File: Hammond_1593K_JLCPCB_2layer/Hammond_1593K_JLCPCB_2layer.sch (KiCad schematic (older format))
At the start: 2 parts

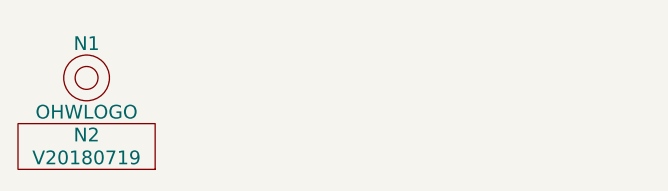
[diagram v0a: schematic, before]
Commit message: added Hammond 1593 PCB outline to template
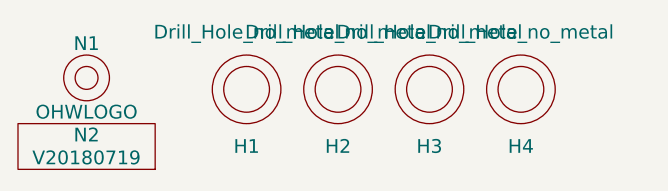
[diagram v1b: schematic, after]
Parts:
- added H1, H2, H3, H4: Drill_Hole_no_metal, SquantorPcbOutline:MountingHole_3.2mm_no_metal, symbol Drill_Hole_no_metal
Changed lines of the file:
@@
 LIBS:SquantorPCBOutline
 LIBS:SquantorProto
-LIBS:jlcpcb_2_layer-cache
+LIBS:Hammond_1593K_JLCPCB_2layer-cache
 EELAYER 25 0
 EELAYER END
@@
 	1    0    0    -1
 $EndComp
+$Comp
+L Drill_Hole_no_metal H1
+U 1 1 5B50D036
+P 1550 7400
+F 0 "H1" H 1550 7150 60  0000 C CNN
+F 1 "Drill_Hole_no_metal" H 1550 7650 60  0000 C CNN
+F 2 "SquantorPcbOutline:MountingHole_3.2mm_no_metal" H 1550 7400 60  0001 C CNN
+F 3 "" H 1550 7400 60  0001 C CNN
+	1    1550 7400
+	1    0    0    -1
+$EndComp
+$Comp
+L Drill_Hole_no_metal H2
+U 1 1 5B50D091
+P 1950 7400
+F 0 "H2" H 1950 7150 60  0000 C CNN
+F 1 "Drill_Hole_no_metal" H 1950 7650 60  0000 C CNN
+F 2 "SquantorPcbOutline:MountingHole_3.2mm_no_metal" H 1950 7400 60  0001 C CNN
+F 3 "" H 1950 7400 60  0001 C CNN
+	1    1950 7400
+	1    0    0    -1
+$EndComp
+$Comp
+L Drill_Hole_no_metal H3
+U 1 1 5B50D0D9
+P 2350 7400
+F 0 "H3" H 2350 7150 60  0000 C CNN
+F 1 "Drill_Hole_no_metal" H 2350 7650 60  0000 C CNN
+F 2 "SquantorPcbOutline:MountingHole_3.2mm_no_metal" H 2350 7400 60  0001 C CNN
+F 3 "" H 2350 7400 60  0001 C CNN
+	1    2350 7400
+	1    0    0    -1
+$EndComp
+$Comp
+L Drill_Hole_no_metal H4
+U 1 1 5B50D104
+P 2750 7400
+F 0 "H4" H 2750 7150 60  0000 C CNN
+F 1 "Drill_Hole_no_metal" H 2750 7650 60  0000 C CNN
+F 2 "SquantorPcbOutline:MountingHole_3.2mm_no_metal" H 2750 7400 60  0001 C CNN
+F 3 "" H 2750 7400 60  0001 C CNN
+	1    2750 7400
+	1    0    0    -1
+$EndComp

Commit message: updated Hammond 1593K JLCPCB 2 layer template
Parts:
- H1, H2, H3, H4: symbol Drill_Hole_no_metal -> SquantorPCBOutline:Drill_Hole_no_metal
- N1: symbol OHWLOGO -> SquantorLabels:OHWLOGO
- N2: value V20180719 -> 20180726; symbol VYYYYMMDD -> SquantorLabels:VYYYYMMDD
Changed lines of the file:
@@
-EESchema Schematic File Version 2
-LIBS:power
-LIBS:device
-LIBS:switches
-LIBS:relays
-LIBS:motors
-LIBS:transistors
-LIBS:conn
-LIBS:linear
-LIBS:regul
-LIBS:74xx
-LIBS:cmos4000
-LIBS:adc-dac
-LIBS:memory
-LIBS:xilinx
-LIBS:microcontrollers
-LIBS:dsp
-LIBS:microchip
-LIBS:analog_switches
-LIBS:motorola
-LIBS:texas
-LIBS:intel
-LIBS:audio
-LIBS:interface
-LIBS:digital-audio
-LIBS:philips
-LIBS:display
-LIBS:cypress
-LIBS:siliconi
-LIBS:opto
-LIBS:atmel
-LIBS:contrib
-LIBS:valves
-LIBS:SquantorButtons
-LIBS:SquantorConnectors
-LIBS:SquantorLabels
-LIBS:SquantorPCBOutline
-LIBS:SquantorProto
+EESchema Schematic File Version 4
 LIBS:Hammond_1593K_JLCPCB_2layer-cache
-EELAYER 25 0
+EELAYER 26 0
 EELAYER END
 $Descr A4 11693 8268
@@
 $EndDescr
 $Comp
-L VYYYYMMDD N2
+L SquantorLabels:VYYYYMMDD N2
 U 1 1 5A1357A5
 P 850 7700
 F 0 "N2" H 850 7800 60  0000 C CNN
-F 1 "V20180719" H 850 7700 60  0000 C CNN
+F 1 "20180726" H 850 7700 60  0000 C CNN
 F 2 "SquantorLabels:Label_version" H 850 7700 60  0001 C CNN
 F 3 "" H 850 7700 60  0001 C CNN
@@
 $EndComp
 $Comp
-L OHWLOGO N1
+L SquantorLabels:OHWLOGO N1
 U 1 1 5A135869
 P 850 7350
@@
 $EndComp
 $Comp
-L Drill_Hole_no_metal H1
+L SquantorPCBOutline:Drill_Hole_no_metal H1
 U 1 1 5B50D036
 P 1550 7400
@@
 $EndComp
 $Comp
-L Drill_Hole_no_metal H2
+L SquantorPCBOutline:Drill_Hole_no_metal H2
 U 1 1 5B50D091
 P 1950 7400
@@
 $EndComp
 $Comp
-L Drill_Hole_no_metal H3
+L SquantorPCBOutline:Drill_Hole_no_metal H3
 U 1 1 5B50D0D9
 P 2350 7400
@@
 $EndComp
 $Comp
-L Drill_Hole_no_metal H4
+L SquantorPCBOutline:Drill_Hole_no_metal H4
 U 1 1 5B50D104
 P 2750 7400
